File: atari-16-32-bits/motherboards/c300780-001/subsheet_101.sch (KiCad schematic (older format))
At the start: 0 parts

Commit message: done u100,u101
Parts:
- added C105, C106: 0.1uF, symbol Device:C
- added R106: 4K7, symbol Device:R_US
- added R111, R112: 0, symbol Device:R_US
- added U101: ST_BLITTER_PHY, Package_LCC:LCC-68_THT-Socket, symbol st_blitter:ST_BLITTER_PHY
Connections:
- new net A1: U101.47 (A1)
- new net A10: U101.56 (A10)
- new net A11: U101.57 (A11)
- new net A12: U101.58 (A12)
- new net A13: U101.59 (A13)
- new net A14: U101.61 (A14)
- new net A15: U101.62 (A15)
- new net A16: U101.63 (A16)
- new net A17: U101.64 (A17)
- new net A18: U101.65 (A18)
- new net A19: U101.66 (A19)
- new net A2: U101.48 (A2)
- new net A20: U101.67 (A20)
- new net A21: U101.2 (A21)
- new net A22: U101.3 (A22)
- new net A23: U101.4 (A23)
- new net A3: U101.49 (A3)
- new net A4: U101.50 (A4)
- new net A5: U101.51 (A5)
- new net A6: U101.52 (A6)
- new net A7: U101.53 (A7)
- new net A8: U101.54 (A8)
- new net A9: U101.55 (A9)
- new net CLK8: U101.34 (CLK)
- new net D0: U101.21 (D0)
- new net D1: U101.20 (D1)
- new net D10: U101.11 (D10)
- new net D11: U101.10 (D11)
- new net D12: U101.9 (D12)
- new net D13: U101.8 (D13)
- new net D14: U101.7 (D14)
- new net D15: U101.6 (D15)
- new net D2: U101.19 (D2)
- new net D3: U101.18 (D3)
- new net D4: U101.17 (D4)
- new net D5: U101.16 (D5)
- new net D6: U101.15 (D6)
- new net D7: U101.14 (D7)
- new net D8: U101.13 (D8)
- new net D9: U101.12 (D9)
- new net FC0: U101.45 (FC0)
- new net FC1: U101.44 (FC1)
- new net GND: C105.2, C106.2, U101.35 (GND), U101.5 (GND)
- new net RXW: U101.26 (R/~W~)
- new net VCC: C105.1, C106.1, R106.1, U101.1 (Vcc), U101.33 (Vcc)
- new net XAS: U101.23 (~AS~)
- new net XBERR: U101.39 (~BERR~)
- new net XBGACK: R112.2, U101.29 (~BGACK~)
- new net XBGK: R106.2, R112.1, U101.40 (~BGKI~)
- new net XBLTBG: R111.1, U101.37 (~BGO~)
- new net XBLTINT: U101.41 (~INT~)
- new net XBR: U101.30 (~BR~)
- new net XCPUBG: R111.2, U101.28 (~BGI~)
- new net XDTACK: U101.27 (~DTACK~)
- new net XLDS: U101.25 (~LDS~)
- new net XRESET: U101.38 (~RESET~)
- new net XUDS: U101.24 (~UDS~)

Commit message: done eprom
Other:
- note added: "R111 and R112 installed\nONLY when \nU101 is NOT installed"
- moved on the sheet: C105, C106, R106, R111, R112
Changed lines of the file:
@@
 L Device:R_US R?
 U 1 1 60962F60
-P 7000 3500
+P 6800 4000
 AR Path="/60786F27/607874AD/60962F60" Ref="R?"  Part="1"
 AR Path="/60786F27/607875AF/60962F60" Ref="R111"  Part="1"
-F 0 "R111" V 7100 3500 50  0000 C CNN
-F 1 "0" V 6900 3500 50  0000 C CNN
-F 2 "" V 7040 3490 50  0001 C CNN
-F 3 "~" H 7000 3500 50  0001 C CNN
-	1    7000 3500
+F 0 "R111" V 6900 4000 50  0000 C CNN
+F 1 "0" V 6700 4000 50  0000 C CNN
+F 2 "" V 6840 3990 50  0001 C CNN
+F 3 "~" H 6800 4000 50  0001 C CNN
+	1    6800 4000
 	0    1    1    0
 $EndComp
@@
 L Device:R_US R?
 U 1 1 60962F66
-P 7000 4000
+P 6800 4500
 AR Path="/60786F27/607874AD/60962F66" Ref="R?"  Part="1"
 AR Path="/60786F27/607875AF/60962F66" Ref="R112"  Part="1"
-F 0 "R112" V 7100 4000 50  0000 C CNN
-F 1 "0" V 6900 4000 50  0000 C CNN
-F 2 "" V 7040 3990 50  0001 C CNN
-F 3 "~" H 7000 4000 50  0001 C CNN
-	1    7000 4000
+F 0 "R112" V 6900 4500 50  0000 C CNN
+F 1 "0" V 6700 4500 50  0000 C CNN
+F 2 "" V 6840 4490 50  0001 C CNN
+F 3 "~" H 6800 4500 50  0001 C CNN
+	1    6800 4500
 	0    1    1    0
 $EndComp
-Text Label 6550 3500 0    50   ~ 0
+Text Label 6350 4000 0    50   ~ 0
 XCPUBG
-Text Label 6550 4000 0    50   ~ 0
+Text Label 6350 4500 0    50   ~ 0
 XBGACK
 $Comp
 L Device:R_US R?
 U 1 1 60985434
-P 7000 3000
+P 6800 3000
 AR Path="/60786F27/607874AD/60985434" Ref="R?"  Part="1"
 AR Path="/60786F27/607875AF/60985434" Ref="R106"  Part="1"
-F 0 "R106" V 7100 3000 50  0000 C CNN
-F 1 "4K7" V 6900 3000 50  0000 C CNN
-F 2 "" V 7040 2990 50  0001 C CNN
-F 3 "~" H 7000 3000 50  0001 C CNN
-	1    7000 3000
+F 0 "R106" V 6900 3000 50  0000 C CNN
+F 1 "4K7" V 6700 3000 50  0000 C CNN
+F 2 "" V 6840 2990 50  0001 C CNN
+F 3 "~" H 6800 3000 50  0001 C CNN
+	1    6800 3000
 	0    1    1    0
 $EndComp
-Text Label 7300 3000 2    50   ~ 0
+Text Label 7100 3000 2    50   ~ 0
 VCC
 Wire Wire Line
-	7300 3000 7150 3000
-Text Label 6650 3000 0    50   ~ 0
+	7100 3000 6950 3000
+Text Label 6450 3000 0    50   ~ 0
 XBGK
 Wire Wire Line
-	6650 3000 6850 3000
+	6450 3000 6650 3000
 Text Label 5200 4250 2    50   ~ 0
 FC0
@@
 L Device:C C?
 U 1 1 609FF3C6
-P 6700 2000
+P 6500 2000
 AR Path="/60786F27/6078774E/609FF3C6" Ref="C?"  Part="1"
 AR Path="/60786F27/607875AF/609FF3C6" Ref="C105"  Part="1"
-F 0 "C105" H 6725 2100 50  0000 L CNN
-F 1 "0.1uF" H 6725 1900 50  0000 L CNN
-F 2 "" H 6738 1850 50  0001 C CNN
-F 3 "~" H 6700 2000 50  0001 C CNN
-	1    6700 2000
+F 0 "C105" H 6525 2100 50  0000 L CNN
+F 1 "0.1uF" H 6525 1900 50  0000 L CNN
+F 2 "" H 6538 1850 50  0001 C CNN
+F 3 "~" H 6500 2000 50  0001 C CNN
+	1    6500 2000
 	1    0    0    -1
 $EndComp
@@
 L Device:C C?
 U 1 1 609FF3CC
-P 7200 2000
+P 7000 2000
 AR Path="/60786F27/6078774E/609FF3CC" Ref="C?"  Part="1"
 AR Path="/60786F27/607875AF/609FF3CC" Ref="C106"  Part="1"
-F 0 "C106" H 7225 2100 50  0000 L CNN
-F 1 "0.1uF" H 7225 1900 50  0000 L CNN
-F 2 "" H 7238 1850 50  0001 C CNN
-F 3 "~" H 7200 2000 50  0001 C CNN
-	1    7200 2000
+F 0 "C106" H 7025 2100 50  0000 L CNN
+F 1 "0.1uF" H 7025 1900 50  0000 L CNN
+F 2 "" H 7038 1850 50  0001 C CNN
+F 3 "~" H 7000 2000 50  0001 C CNN
+	1    7000 2000
 	1    0    0    -1
 $EndComp
-Text Label 6700 2150 3    50   ~ 0
+Text Label 6500 2150 3    50   ~ 0
 GND
-Text Label 7200 2150 3    50   ~ 0
+Text Label 7000 2150 3    50   ~ 0
 GND
-Text Label 6700 1850 1    50   ~ 0
+Text Label 6500 1850 1    50   ~ 0
 VCC
-Text Label 7200 1850 1    50   ~ 0
+Text Label 7000 1850 1    50   ~ 0
 VCC
 Wire Wire Line
-	6550 3500 6850 3500
-Wire Wire Line
-	6550 4000 6850 4000
-Text Label 7450 3500 2    50   ~ 0
+	6350 4000 6650 4000
+Wire Wire Line
+	6350 4500 6650 4500
+Text Label 7250 4000 2    50   ~ 0
 XBLTBG
 Wire Wire Line
-	7150 3500 7450 3500
-Text Label 7350 4000 2    50   ~ 0
+	6950 4000 7250 4000
+Text Label 7150 4500 2    50   ~ 0
 XBGK
 Wire Wire Line
-	7350 4000 7150 4000
+	7150 4500 6950 4500
+Text Notes 6300 3700 0    50   ~ 0
+R111 and R112 installed\nONLY when \nU101 is NOT installed
+Wire Notes Line
+	6250 3400 7300 3400
+Wire Notes Line
+	7300 3400 7300 4700
+Wire Notes Line
+	7300 4700 6250 4700
+Wire Notes Line
+	6250 4700 6250 3400
 $EndSCHEMATC

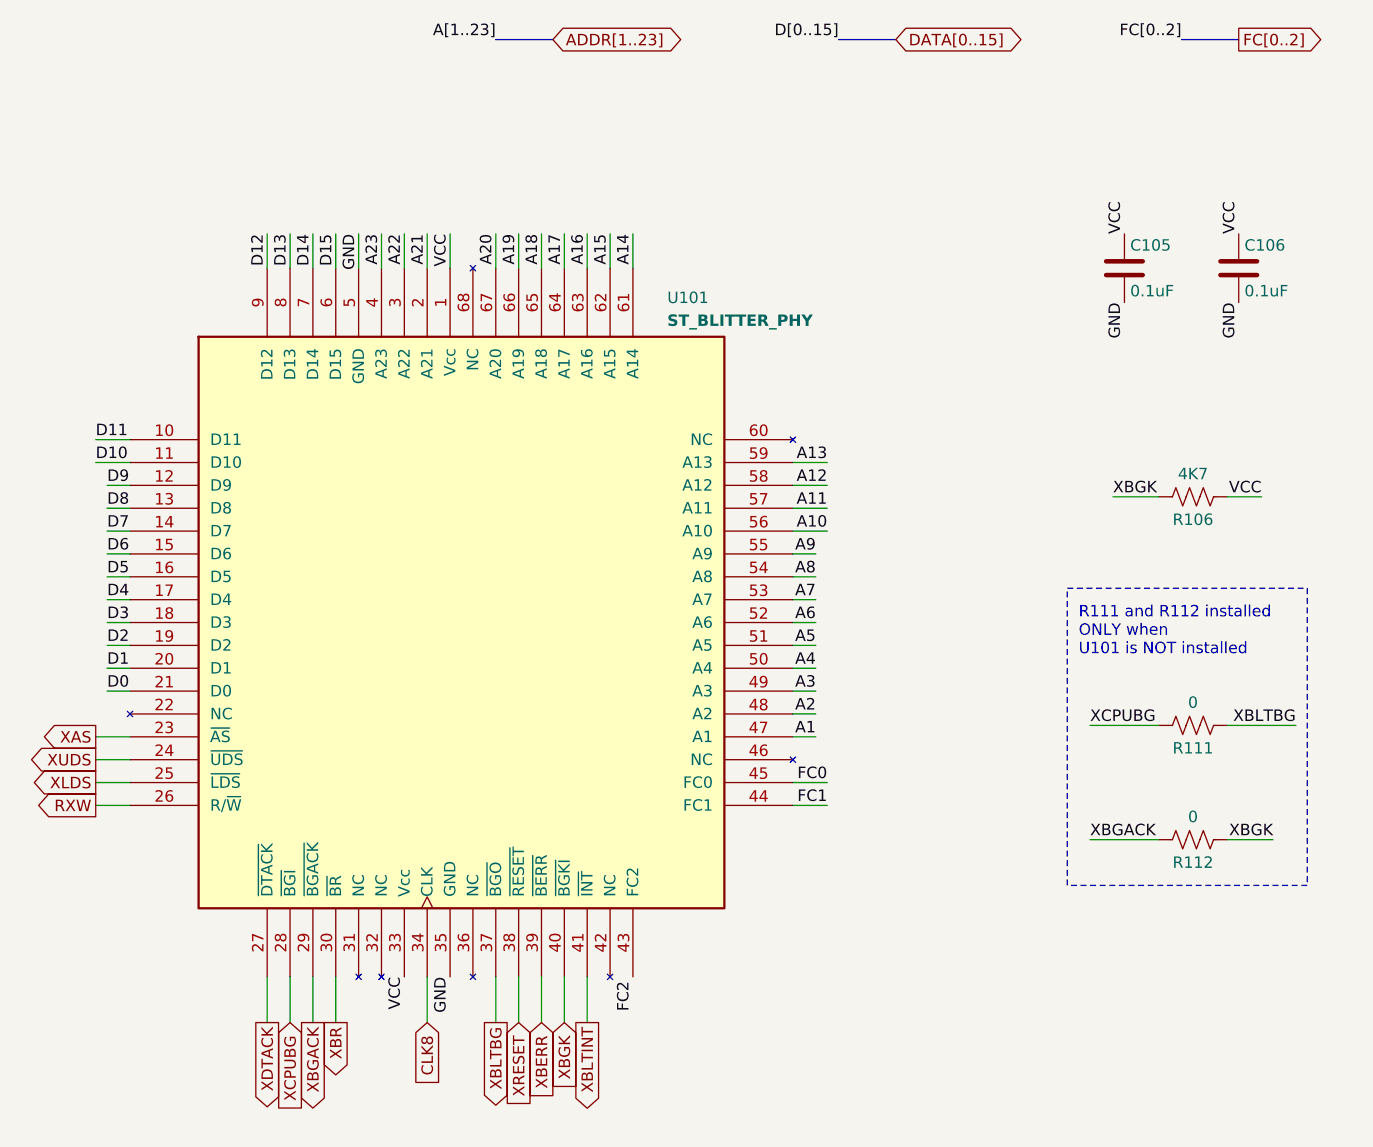
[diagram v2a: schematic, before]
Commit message: reorganized sheets
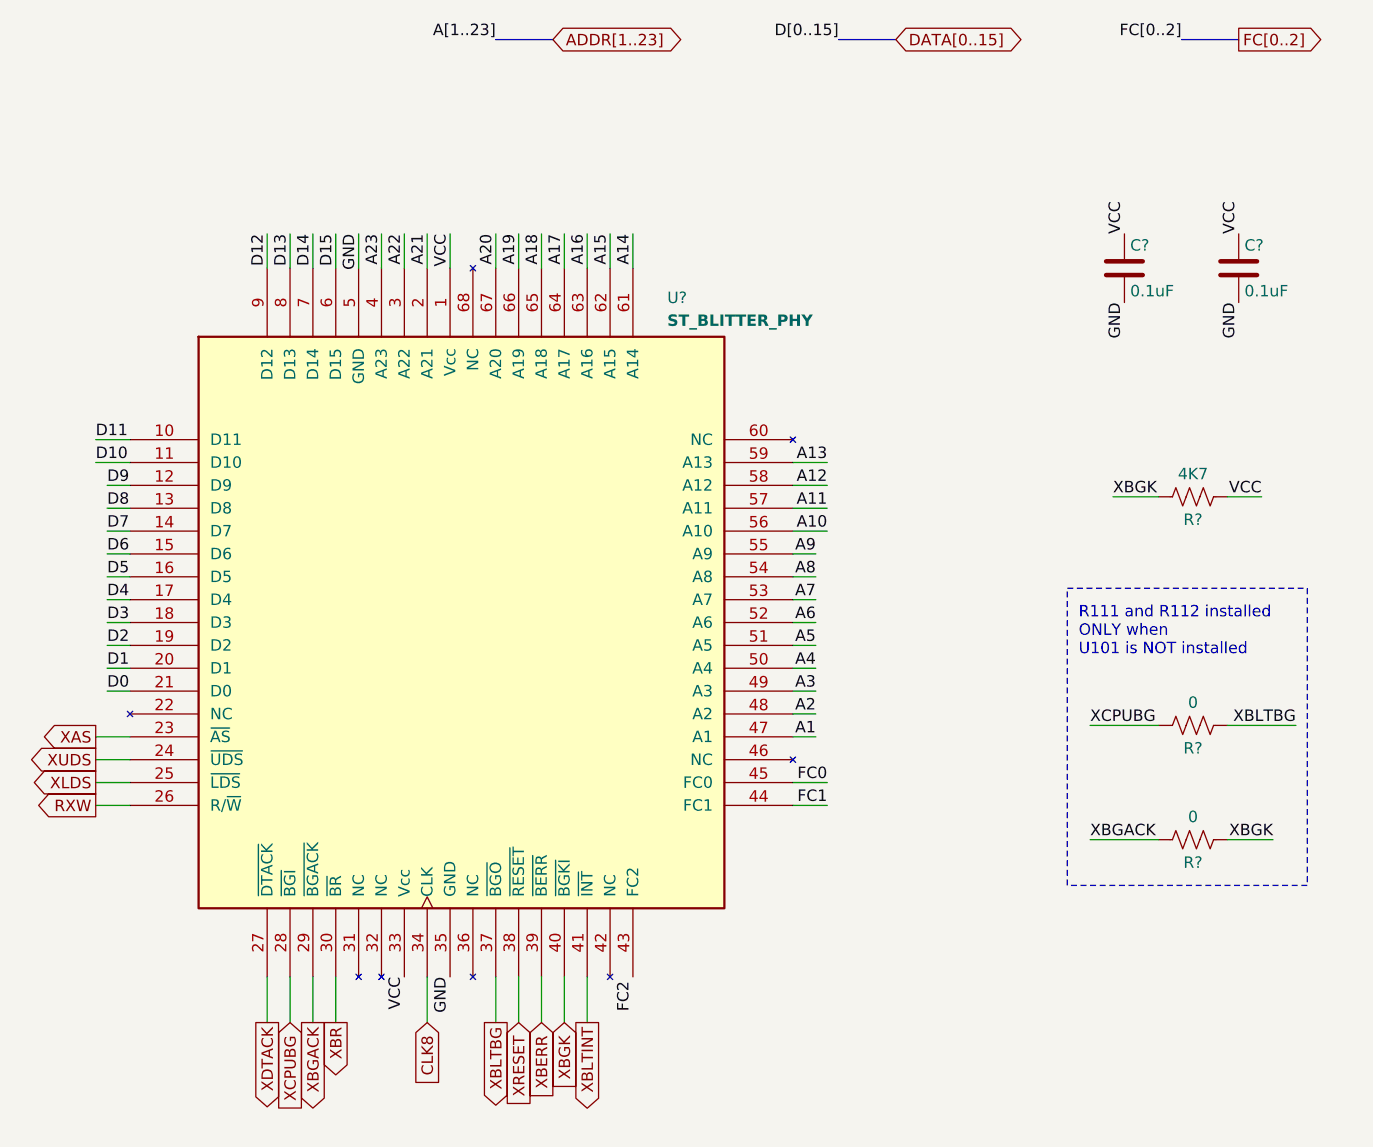
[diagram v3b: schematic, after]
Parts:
- renumbered U101 to U?
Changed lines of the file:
@@
 $Descr A4 8268 11693 portrait
 encoding utf-8
-Sheet 4 14
+Sheet 8 8
 Title ""
 Date ""
@@
 $EndDescr
 $Comp
-L st_blitter:ST_BLITTER_PHY U101
+L st_blitter:ST_BLITTER_PHY U?
 U 1 1 607AE185
 P 3600 3550
-F 0 "U101" H 4500 5000 50  0000 L TNN
+F 0 "U?" H 4500 5000 50  0000 L TNN
 F 1 "ST_BLITTER_PHY" H 4500 4900 50  0000 L TNB
 F 2 "Package_LCC:LCC-68_THT-Socket" H 4500 5100 50  0001 L TNN
@@
 AR Path="/60786F27/607874AD/60962F60" Ref="R?"  Part="1"
 AR Path="/60786F27/607875AF/60962F60" Ref="R111"  Part="1"
-F 0 "R111" V 6900 4000 50  0000 C CNN
+AR Path="/6089D0BA/60962F60" Ref="R?"  Part="1"
+F 0 "R?" V 6900 4000 50  0000 C CNN
 F 1 "0" V 6700 4000 50  0000 C CNN
 F 2 "" V 6840 3990 50  0001 C CNN
@@
 AR Path="/60786F27/607874AD/60962F66" Ref="R?"  Part="1"
 AR Path="/60786F27/607875AF/60962F66" Ref="R112"  Part="1"
-F 0 "R112" V 6900 4500 50  0000 C CNN
+AR Path="/6089D0BA/60962F66" Ref="R?"  Part="1"
+F 0 "R?" V 6900 4500 50  0000 C CNN
 F 1 "0" V 6700 4500 50  0000 C CNN
 F 2 "" V 6840 4490 50  0001 C CNN
@@
 AR Path="/60786F27/607874AD/60985434" Ref="R?"  Part="1"
 AR Path="/60786F27/607875AF/60985434" Ref="R106"  Part="1"
-F 0 "R106" V 6900 3000 50  0000 C CNN
+AR Path="/6089D0BA/60985434" Ref="R?"  Part="1"
+F 0 "R?" V 6900 3000 50  0000 C CNN
 F 1 "4K7" V 6700 3000 50  0000 C CNN
 F 2 "" V 6840 2990 50  0001 C CNN
@@
 AR Path="/60786F27/6078774E/609FF3C6" Ref="C?"  Part="1"
 AR Path="/60786F27/607875AF/609FF3C6" Ref="C105"  Part="1"
-F 0 "C105" H 6525 2100 50  0000 L CNN
+AR Path="/6089D0BA/609FF3C6" Ref="C?"  Part="1"
+F 0 "C?" H 6525 2100 50  0000 L CNN
 F 1 "0.1uF" H 6525 1900 50  0000 L CNN
 F 2 "" H 6538 1850 50  0001 C CNN
@@
 AR Path="/60786F27/6078774E/609FF3CC" Ref="C?"  Part="1"
 AR Path="/60786F27/607875AF/609FF3CC" Ref="C106"  Part="1"
-F 0 "C106" H 7025 2100 50  0000 L CNN
+AR Path="/6089D0BA/609FF3CC" Ref="C?"  Part="1"
+F 0 "C?" H 7025 2100 50  0000 L CNN
 F 1 "0.1uF" H 7025 1900 50  0000 L CNN
 F 2 "" H 7038 1850 50  0001 C CNN

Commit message: re-annotate component following move of subsheets in schematics
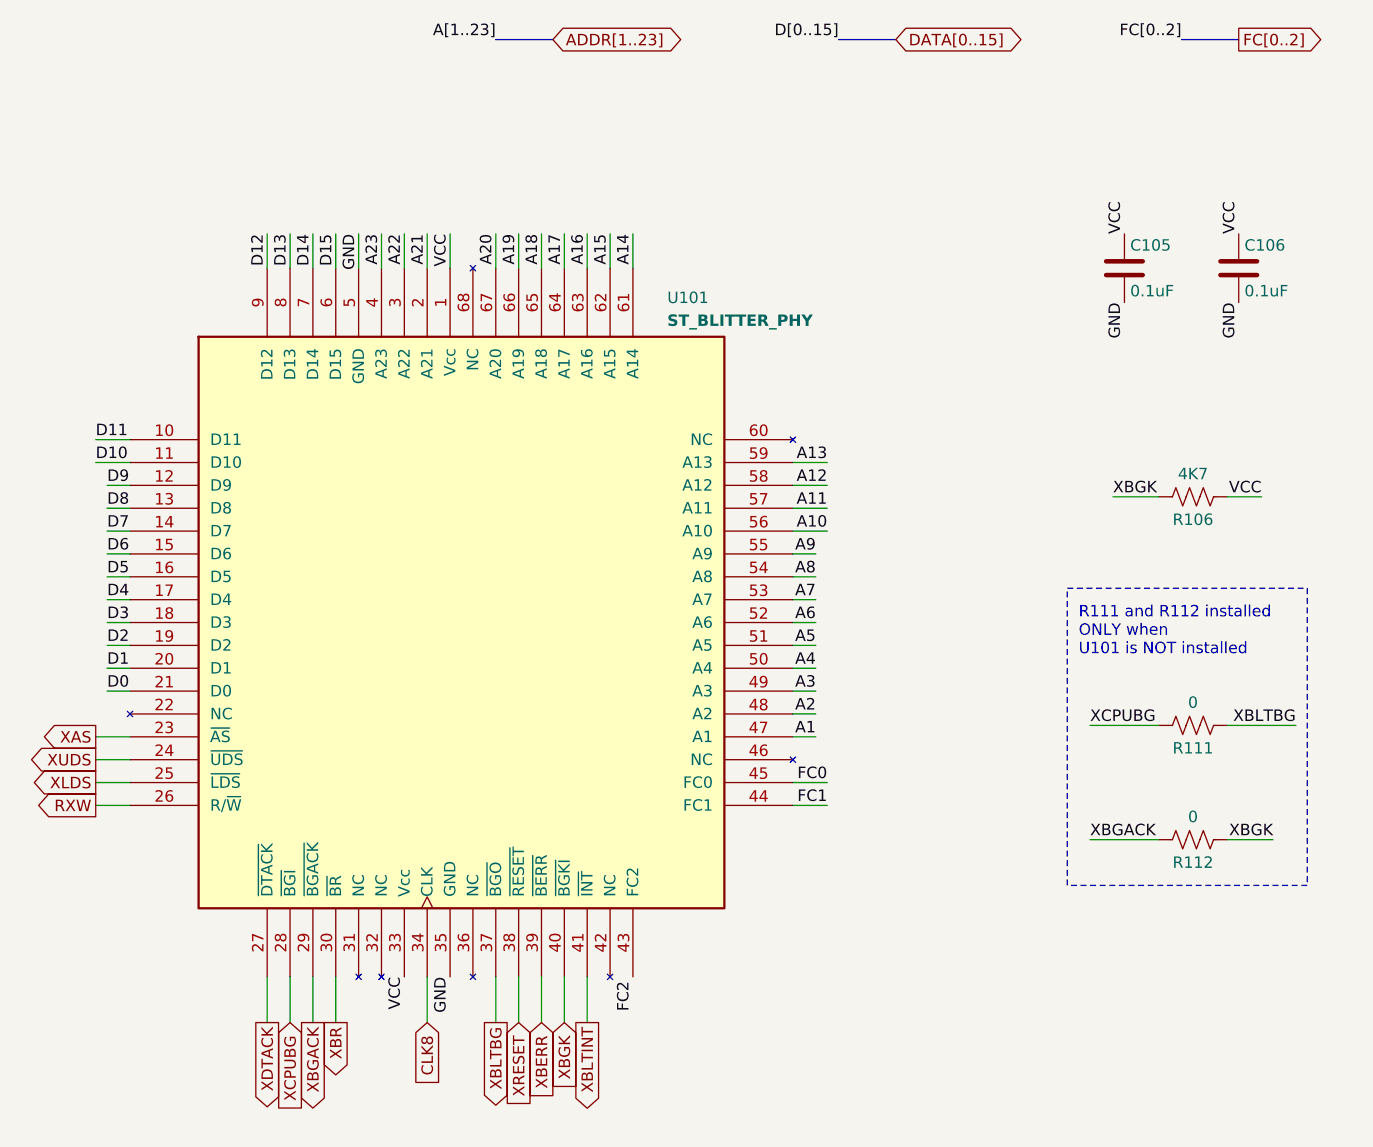
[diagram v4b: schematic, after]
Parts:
- gave numbers to parts that had none: 1
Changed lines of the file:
@@
 $Descr A4 8268 11693 portrait
 encoding utf-8
-Sheet 8 8
+Sheet 2 9
 Title ""
 Date ""
@@
 $EndDescr
 $Comp
-L st_blitter:ST_BLITTER_PHY U?
+L st_blitter:ST_BLITTER_PHY U101
 U 1 1 607AE185
 P 3600 3550
-F 0 "U?" H 4500 5000 50  0000 L TNN
+F 0 "U101" H 4500 5000 50  0000 L TNN
 F 1 "ST_BLITTER_PHY" H 4500 4900 50  0000 L TNB
 F 2 "Package_LCC:LCC-68_THT-Socket" H 4500 5100 50  0001 L TNN
@@
 AR Path="/60786F27/607874AD/60962F60" Ref="R?"  Part="1"
 AR Path="/60786F27/607875AF/60962F60" Ref="R111"  Part="1"
-AR Path="/6089D0BA/60962F60" Ref="R?"  Part="1"
-F 0 "R?" V 6900 4000 50  0000 C CNN
+AR Path="/6089D0BA/60962F60" Ref="R111"  Part="1"
+F 0 "R111" V 6900 4000 50  0000 C CNN
 F 1 "0" V 6700 4000 50  0000 C CNN
 F 2 "" V 6840 3990 50  0001 C CNN
@@
 AR Path="/60786F27/607874AD/60962F66" Ref="R?"  Part="1"
 AR Path="/60786F27/607875AF/60962F66" Ref="R112"  Part="1"
-AR Path="/6089D0BA/60962F66" Ref="R?"  Part="1"
-F 0 "R?" V 6900 4500 50  0000 C CNN
+AR Path="/6089D0BA/60962F66" Ref="R112"  Part="1"
+F 0 "R112" V 6900 4500 50  0000 C CNN
 F 1 "0" V 6700 4500 50  0000 C CNN
 F 2 "" V 6840 4490 50  0001 C CNN
@@
 AR Path="/60786F27/607874AD/60985434" Ref="R?"  Part="1"
 AR Path="/60786F27/607875AF/60985434" Ref="R106"  Part="1"
-AR Path="/6089D0BA/60985434" Ref="R?"  Part="1"
-F 0 "R?" V 6900 3000 50  0000 C CNN
+AR Path="/6089D0BA/60985434" Ref="R106"  Part="1"
+F 0 "R106" V 6900 3000 50  0000 C CNN
 F 1 "4K7" V 6700 3000 50  0000 C CNN
 F 2 "" V 6840 2990 50  0001 C CNN
@@
 AR Path="/60786F27/6078774E/609FF3C6" Ref="C?"  Part="1"
 AR Path="/60786F27/607875AF/609FF3C6" Ref="C105"  Part="1"
-AR Path="/6089D0BA/609FF3C6" Ref="C?"  Part="1"
-F 0 "C?" H 6525 2100 50  0000 L CNN
+AR Path="/6089D0BA/609FF3C6" Ref="C105"  Part="1"
+F 0 "C105" H 6525 2100 50  0000 L CNN
 F 1 "0.1uF" H 6525 1900 50  0000 L CNN
 F 2 "" H 6538 1850 50  0001 C CNN
@@
 AR Path="/60786F27/6078774E/609FF3CC" Ref="C?"  Part="1"
 AR Path="/60786F27/607875AF/609FF3CC" Ref="C106"  Part="1"
-AR Path="/6089D0BA/609FF3CC" Ref="C?"  Part="1"
-F 0 "C?" H 7025 2100 50  0000 L CNN
+AR Path="/6089D0BA/609FF3CC" Ref="C106"  Part="1"
+F 0 "C106" H 7025 2100 50  0000 L CNN
 F 1 "0.1uF" H 7025 1900 50  0000 L CNN
 F 2 "" H 7038 1850 50  0001 C CNN
